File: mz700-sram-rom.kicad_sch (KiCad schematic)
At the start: 19 parts, among them J1 JTAG, J2 MZ700Bus-2014-single-row, SW1 SW_DIP_x05, U1 ATF1502-44, U2 74HCT688, U3 74HCT670, U4 74HCT670, U5 AS6C1008, U6 28C64

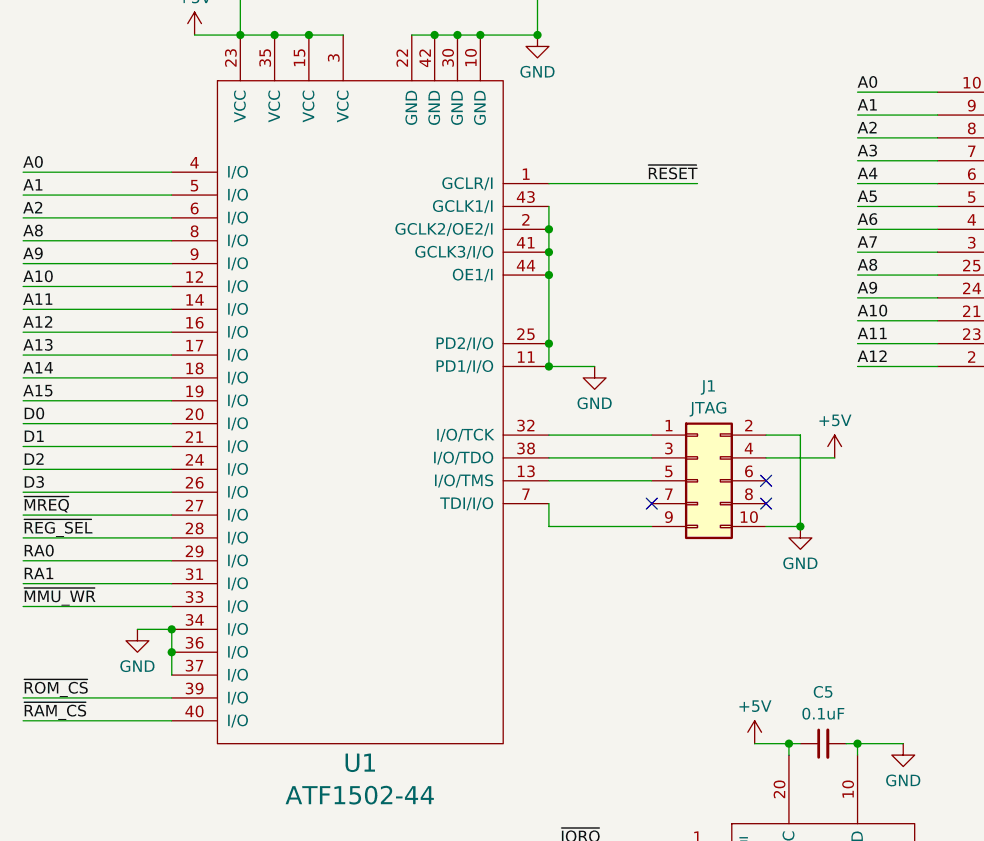
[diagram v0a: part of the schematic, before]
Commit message: 1.3
Added logic to disable the board is $D000->$FFFF is locked ($E5) or DRAM ($E1)
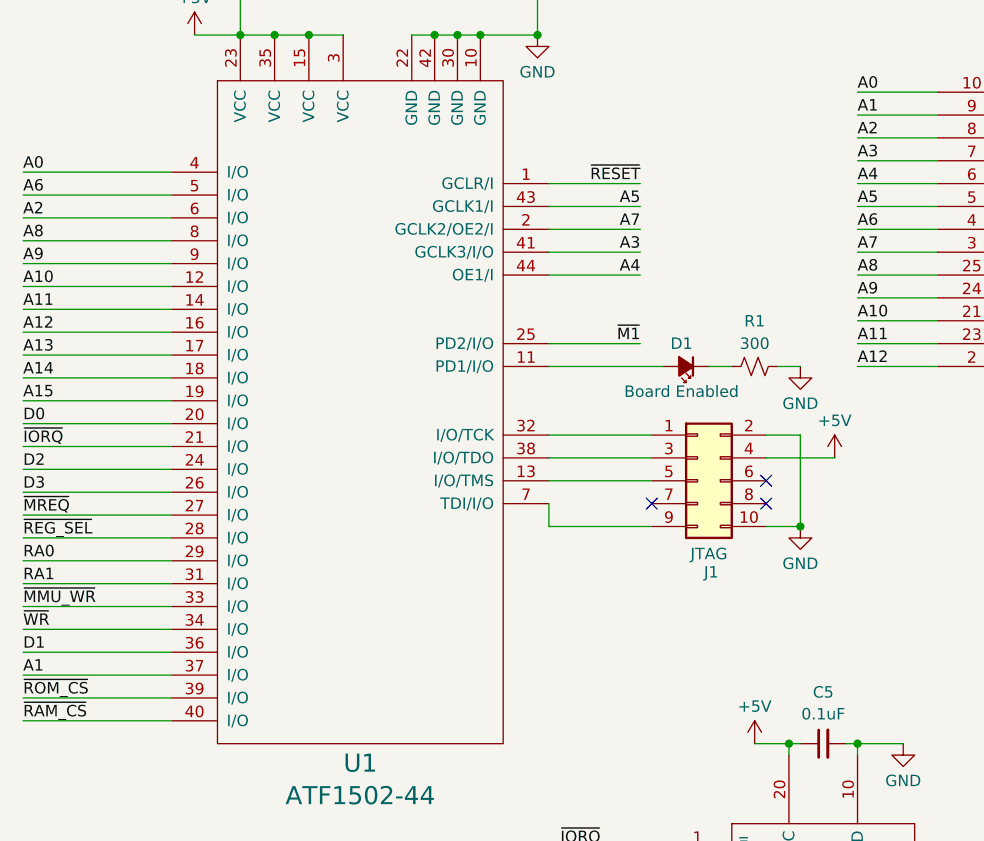
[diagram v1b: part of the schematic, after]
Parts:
- added D1: Board Enabled, LED_THT:LED_D5.0mm, symbol Device:LED_Small_Filled
- added R1: 300, Resistor_THT:R_Axial_DIN0204_L3.6mm_D1.6mm_P5.08mm_Horizontal, symbol Device:R_Small_US
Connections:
- net A1: now also U1.37 (I/O); no longer U1.5 (I/O)
- net A3: now also U1.41 (GCLK3/I/O)
- net A4: now also U1.44 (OE1/I)
- net A5: now also U1.43 (GCLK1/I)
- net A6: now also U1.5 (I/O)
- net A7: now also U1.2 (GCLK2/OE2/I)
- net D1: now also U1.36 (I/O); no longer U1.21 (I/O)
- net GND: now also R1.2; no longer U1.11 (PD1/I/O), U1.2 (GCLK2/OE2/I), U1.25 (PD2/I/O), U1.34 (I/O), U1.36 (I/O), U1.37 (I/O), U1.41 (GCLK3/I/O), U1.43 (GCLK1/I), U1.44 (OE1/I)
- net ~{IORQ}: now also U1.21 (I/O)
- net ~{M1}: now also U1.25 (PD2/I/O)
- net ~{WR}: now also U1.34 (I/O)
- new net: D1.1 (K), R1.1
- new net: D1.2 (A), U1.11 (PD1/I/O)

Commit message: added board id
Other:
- company: (none) -> TBC
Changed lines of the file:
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@@
 		(date "2024-05-19")
 		(rev "1.0")
+		(company "TBC")
+		(comment 1 "ST-401")
 	)
 	(junction

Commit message: cleanup
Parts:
- D1: footprint LED_THT:LED_D5.0mm -> LED_THT:LED_D3.0mm
- J2: symbol sharpox:MZ700Bus-2014-single-row -> sharpox:MZ700Bus-2014_single-row
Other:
- moved on the sheet: J2
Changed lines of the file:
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@@
 	)
 	(junction
+		(at 302.26 69.85)
+		(diameter 0)
+		(color 0 0 0 0)
+	)
+	(junction
 		(at 204.47 71.12)
 		(diameter 0)
@@
 	)
 	(junction
+		(at 302.26 81.28)
+		(diameter 0)
+		(color 0 0 0 0)
+	)
+	(junction
 		(at 72.39 19.05)
 		(diameter 0)
@@
 			)
 		)
-		(property "Footprint" "LED_THT:LED_D5.0mm"
+		(property "Footprint" "LED_THT:LED_D3.0mm"
 			(at 102.87 66.04 90)
 			(effects
@@
 	)
 	(symbol
-		(lib_id "sharpox:MZ700Bus-2014-single-row")
+		(lib_id "sharpox:MZ700Bus-2014_single-row")
 		(at 328.93 72.39 0)
 		(unit 1)
@@
 		)
 		(property "Footprint" "Connector_PinSocket_2.54mm:PinSocket_1x34_P2.54mm_Vertical"
-			(at 332.74 119.38 0)
+			(at 332.74 118.11 0)
 			(effects
 				(font
@@
 			)
 		)
-		(property "Description" "Sharp MZ700 1x34 single row connector (RC2014 compatible)"
-			(at 328.93 72.39 0)
+		(property "Description" "1x34 connector"
+			(at 331.47 120.142 0)
 			(effects
 				(font
@@
 	)
 	(symbol
+		(lib_id "power:PWR_FLAG")
+		(at 302.26 69.85 0)
+		(unit 1)
+		(exclude_from_sim no)
+		(in_bom yes)
+		(on_board yes)
+		(dnp no)
+		(fields_autoplaced yes)
+		(property "Reference" "#FLG01"
+			(at 302.26 67.945 0)
+			(effects
+				(font
+					(size 1.27 1.27)
+				)
+				(hide yes)
+			)
+		)
+		(property "Value" "PWR_FLAG"
+			(at 302.26 65.7169 0)
+			(effects
+				(font
+					(size 1.27 1.27)
+				)
+			)
+		)
+		(property "Footprint" ""
+			(at 302.26 69.85 0)
+			(effects
+				(font
+					(size 1.27 1.27)
+				)
+				(hide yes)
+			)
+		)
+		(property "Datasheet" "~"
+			(at 302.26 69.85 0)
+			(effects
+				(font
+					(size 1.27 1.27)
+				)
+				(hide yes)
+			)
+		)
+		(property "Description" "Special symbol for telling ERC where power comes from"
+			(at 302.26 69.85 0)
+			(effects
+				(font
+					(size 1.27 1.27)
+				)
+				(hide yes)
+			)
+		)
+		(pin "1"
+		)
+		(instances
+			(project ""
+				(path "/d264b6a0-4c73-4c34-b78d-e7c4e07912b7"
+					(reference "#FLG01")
+					(unit 1)
+				)
+			)
+		)
+	)
+	(symbol
 		(lib_id "power:GND")
 		(at 142.24 22.86 0)
@@
 					(unit 1)
 				)
+			)
+		)
+	)
+	(symbol
+		(lib_id "power:PWR_FLAG")
+		(at 302.26 81.28 180)
+		(unit 1)
+		(exclude_from_sim no)
+		(in_bom yes)
+		(on_board yes)
+		(dnp no)
+		(fields_autoplaced yes)
+		(property "Reference" "#FLG02"
+			(at 302.26 83.185 0)
+			(effects
+				(font
+					(size 1.27 1.27)
+				)
+				(hide yes)
+			)
+		)
+		(property "Value" "PWR_FLAG"
+			(at 302.26 85.4131 0)
+			(effects
+				(font
+					(size 1.27 1.27)
+				)
+			)
+		)
+		(property "Footprint" ""
+			(at 302.26 81.28 0)
+			(effects
+				(font
+					(size 1.27 1.27)
+				)
+				(hide yes)
+			)
+		)
+		(property "Datasheet" "~"
+			(at 302.26 81.28 0)
+			(effects
+				(font
+					(size 1.27 1.27)
+				)
+				(hide yes)
+			)
+		)
+		(property "Description" "Special symbol for telling ERC where power comes from"
+			(at 302.26 81.28 0)
+			(effects
+				(font
+					(size 1.27 1.27)
+				)
+				(hide yes)
+			)
+		)
+		(pin "1"
+		)
+		(instances
+			(project ""
+				(path "/d264b6a0-4c73-4c34-b78d-e7c4e07912b7"
+					(reference "#FLG02")
+					(unit 1)
+				)

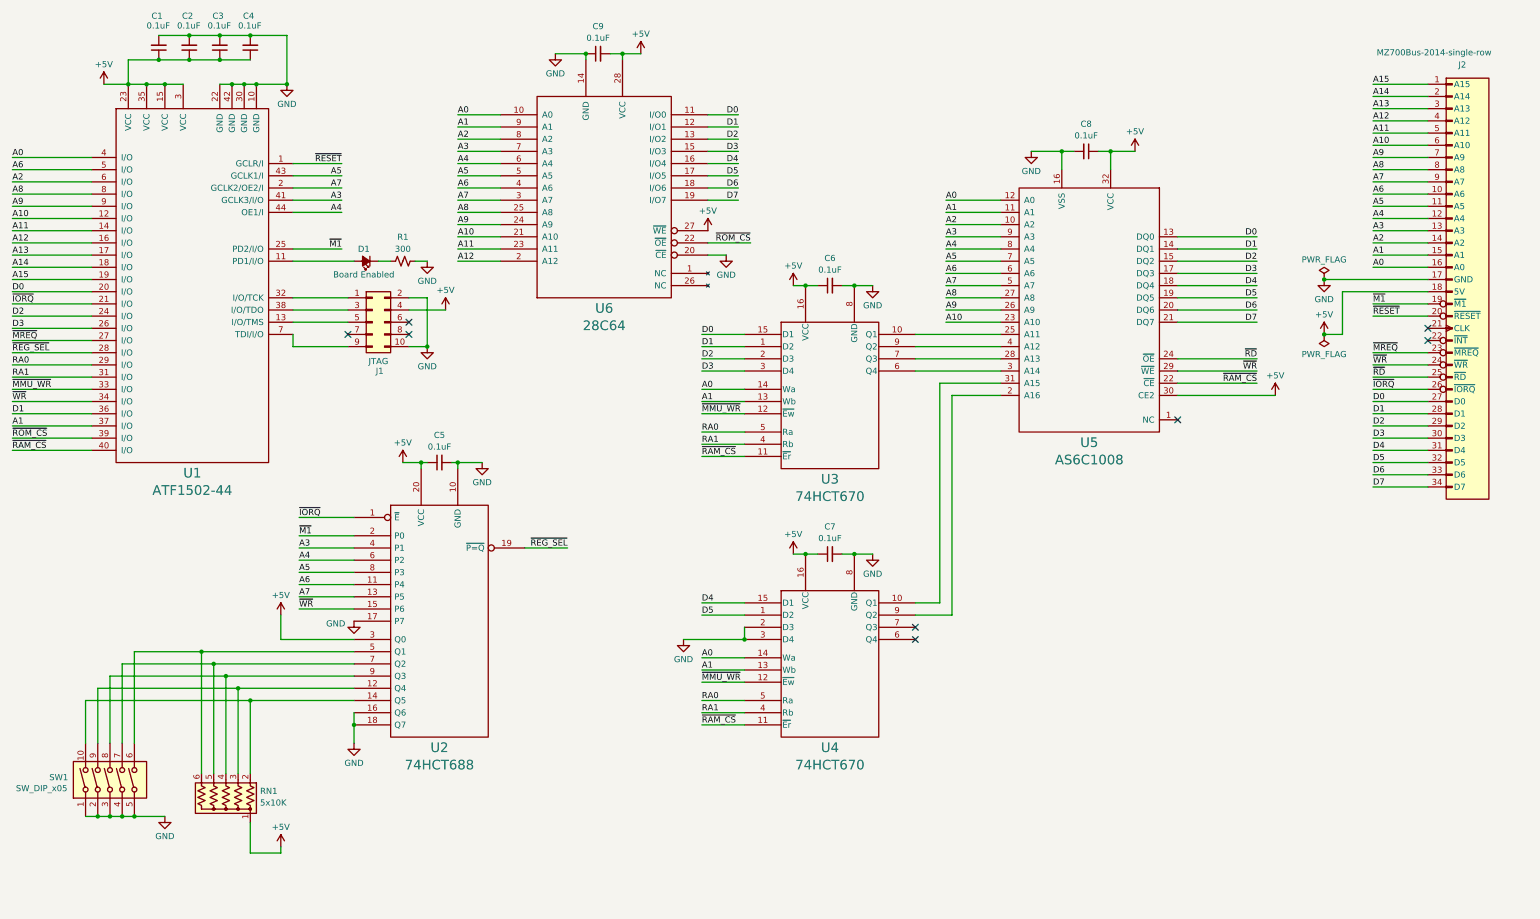
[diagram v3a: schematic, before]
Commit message: replaced LED from cpld with transistor
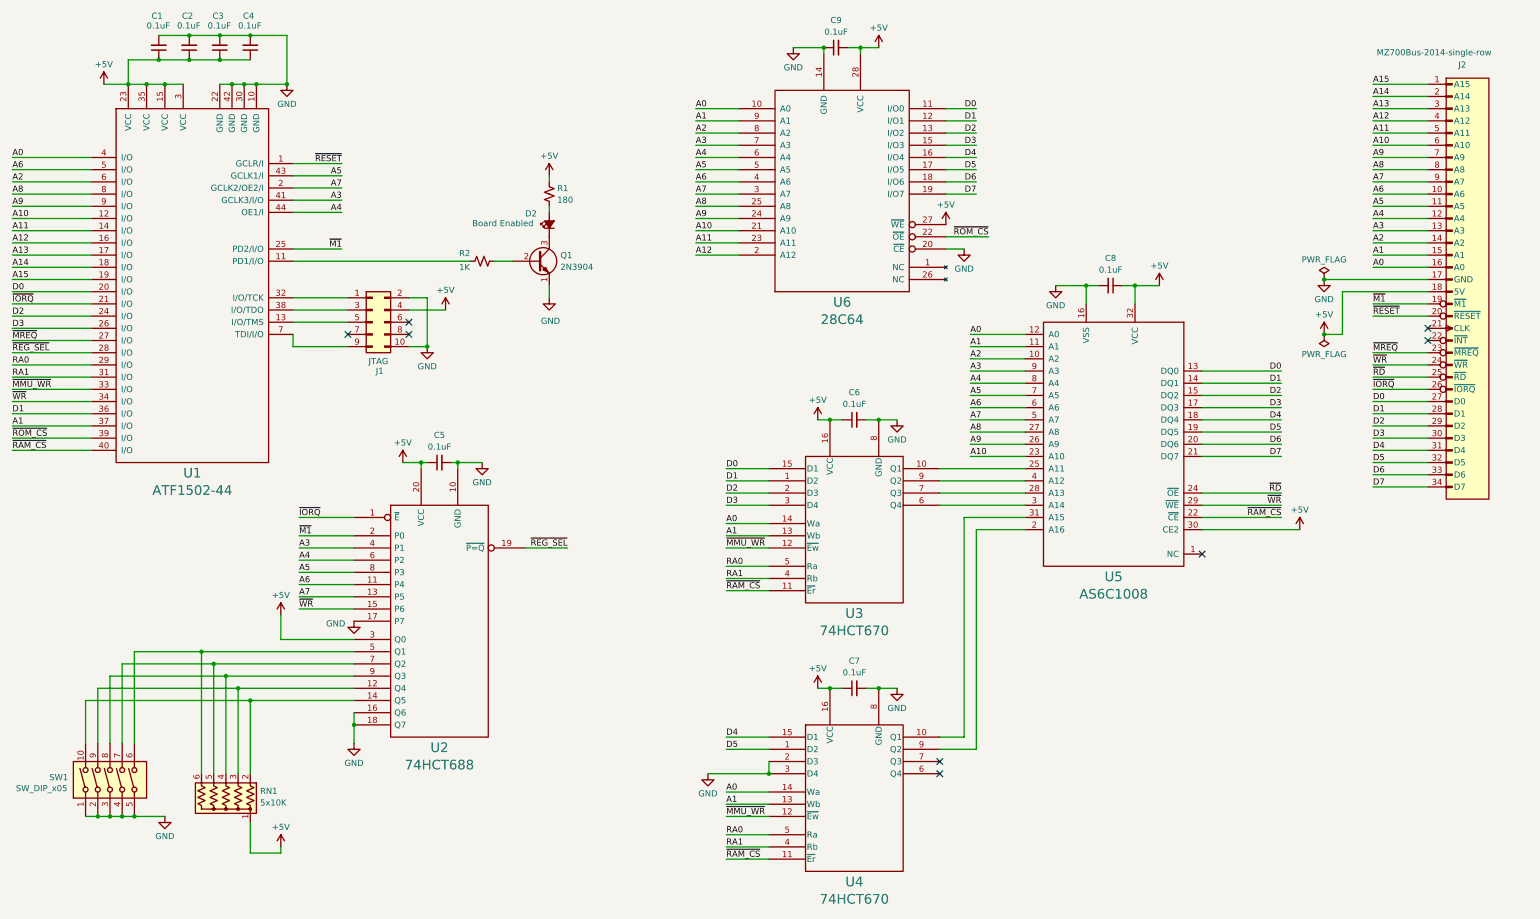
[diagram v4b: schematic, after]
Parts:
- removed D1: Board Enabled, LED_THT:LED_D3.0mm, symbol Device:LED_Small_Filled
- added D2: Board Enabled, LED_THT:LED_D3.0mm, symbol Device:LED_Small_Filled
- added Q1: 2N3904, Package_TO_SOT_THT:TO-92_Inline, symbol Transistor_BJT:2N3904
- added R2: 1K, Resistor_THT:R_Axial_DIN0204_L3.6mm_D1.6mm_P7.62mm_Horizontal, symbol Device:R_Small_US
- R1: value 300 -> 180; footprint Resistor_THT:R_Axial_DIN0204_L3.6mm_D1.6mm_P5.08mm_Horizontal -> Resistor_THT:R_Axial_DIN0204_L3.6mm_D1.6mm_P7.62mm_Horizontal
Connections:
- net +5V: now also R1.1
- net GND: now also Q1.1 (E); no longer R1.2
- net at U1.11 (PD1/I/O): now also R2.1
- new net: Q1.2 (B), R2.2
- new net: D2.1 (K), Q1.3 (C)
- new net: D2.2 (A), R1.2
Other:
- moved on the sheet: C6, C7, C8, C9, U3, U4, U5, U6
